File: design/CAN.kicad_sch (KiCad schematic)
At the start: 4 parts, among them U401 SN65HVD232

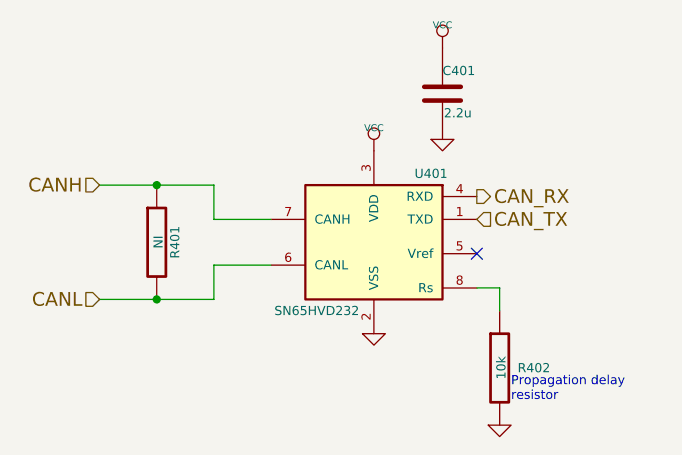
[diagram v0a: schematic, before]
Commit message: v 4.13 produced by jlcpcb
Some serious issues with usb connectors facing the caps. Working fine
otherwise
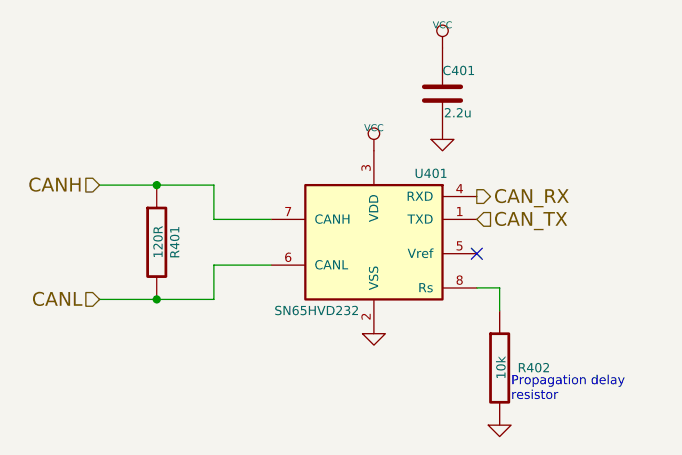
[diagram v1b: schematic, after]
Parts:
- C401: JLCPCB (none) -> C23630
- R401: value NI -> 120R
- U401: JLCPCB (none) -> C30530
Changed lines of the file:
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@@
 (kicad_sch
-	(version 20231120)
+	(version 20250114)
 	(generator "eeschema")
-	(generator_version "8.0")
+	(generator_version "9.0")
 	(paper "A4")
 	(title_block
 		(title "BLDC Driver 4.11")
 		(date "21 aug 2015")
-		(rev "4.12")
+		(rev "${version}")
 		(company "Benjamin Vedder")
+	)
+	(text "Propagation delay\nresistor"
+		(exclude_from_sim no)
+		(at 163.83 120.65 0)
+		(effects
+			(font
+				(size 1.016 1.016)
+			)
+			(justify left bottom)
+		)
 	)
 	(junction
@@
 		)
 	)
-	(text "Propagation delay\nresistor"
-		(exclude_from_sim no)
-		(at 163.83 120.65 0)
-		(effects
-			(font
-				(size 1.016 1.016)
-			)
-			(justify left bottom)
-		)
-	)
 	(hierarchical_label "CANL"
 		(shape input)
 		(at 118.11 109.22 180)
-		(fields_autoplaced yes)
 		(effects
 			(font
@@
 		(shape input)
 		(at 118.11 96.52 180)
-		(fields_autoplaced yes)
 		(effects
 			(font
@@
 		(shape output)
 		(at 160.02 97.79 0)
-		(fields_autoplaced yes)
 		(effects
 			(font
@@
 		(shape input)
 		(at 160.02 100.33 0)
-		(fields_autoplaced yes)
 		(effects
 			(font
@@
 			)
 		)
+		(property "JLCPCB" "C30530"
+			(at 148.59 102.87 0)
+			(effects
+				(font
+					(size 1.27 1.27)
+				)
+				(hide yes)
+			)
+		)
 		(pin "1"
 		)
@@
 			)
 		)
+		(property "JLCPCB" "C23630"
+			(at 156.21 86.36 0)
+			(effects
+				(font
+					(size 1.27 1.27)
+				)
+				(hide yes)
+			)
+		)
 		(pin "1"
 		)
@@
 			)
 		)
-		(property "Value" "NI"
+		(property "Value" "120R"
 			(at 124.6378 102.8446 90)
 			(effects
